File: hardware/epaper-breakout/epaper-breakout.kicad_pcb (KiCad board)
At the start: 2 copper layers, 100 x 40.5 mm, 90 parts, among them J1 XF2M-3315-1A, J2 C10418, J3 Conn_02x06_Counter_Clockwise, J4 ED060SC4, J5 Conn_01x01_Male, J6 Conn_01x01_Male, Q1 AO3401A, Q2 AO3401A, Q3 MMBT3904, Q4 MMBT3904, Q5 AO3401A, Q6 MMBT3904, U1 MCP1700-3302E_SOT23, U10 ED060SC7, U11 TP4056, U12 CH340C, U2 LT1945, U3 LT1945, U4 XC6206PxxxMR, U5 ESP32-WROVER, U6 ED060XC5, U7 LM358, U8 74HC4094-normal, U9 MCP9700AT-ETT

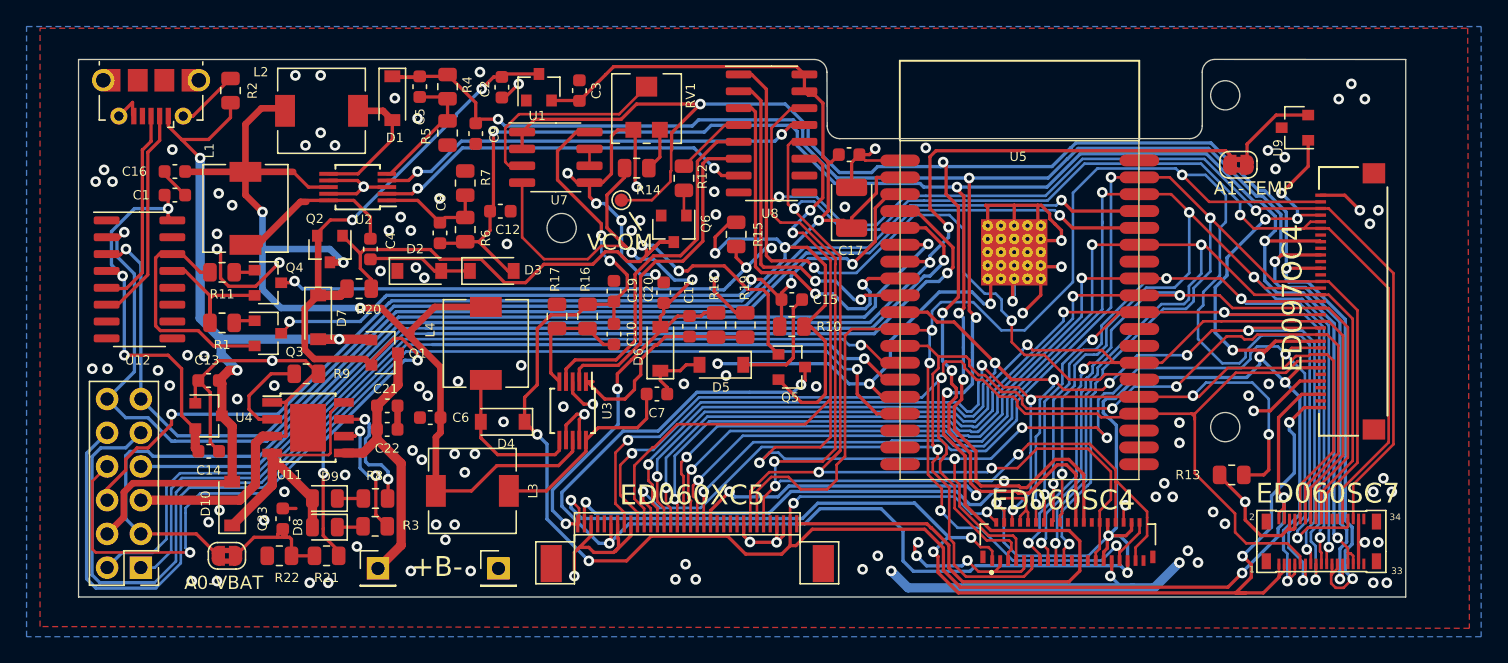
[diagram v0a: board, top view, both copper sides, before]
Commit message: minor change in V5
exchange L1 <-> U2 position
change usb connector footprint
change U6 footprint
chang RV1 footprint
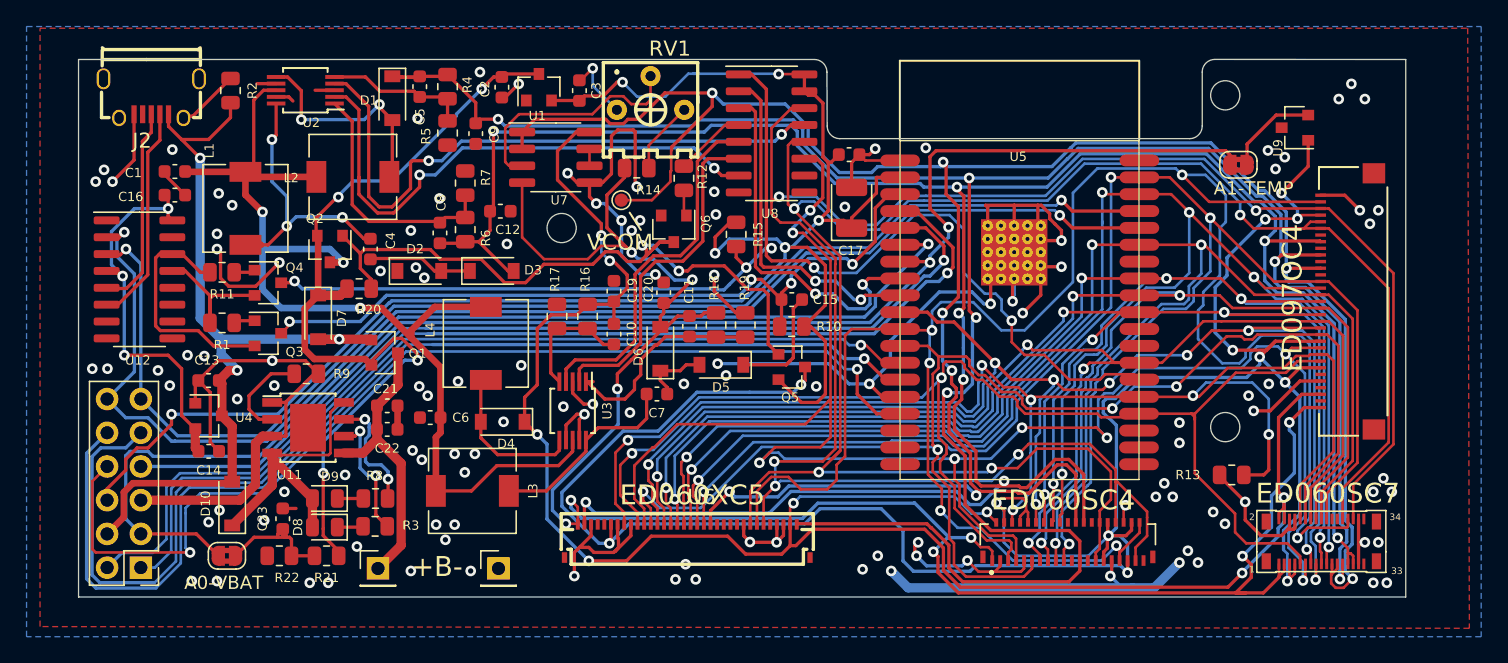
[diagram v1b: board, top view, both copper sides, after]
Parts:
- J2: footprint epaper-breakout:USB_Micro-B_A01SB141B1-067 -> epaper-breakout:JLC_MICRO-USB-SMD_A4A0507-E-01-R
- RV1: footprint epaper-breakout:EVM3ESX50B25 -> epaper-breakout:JLC_RES-ADJ-TH_3362P
- U6: footprint epaper-breakout:X05A20H34G -> epaper-breakout:JLC_FFC-SMD_34P-P0.50_FH34SRJ-34S-0.5SH
- moved U2 8.30 mm to (42.1, 21.8)
- moved L2 5.51 mm to (45.7, 28.3)
- moved J2 1.36 mm to (30.5, 22.4)
- moved U6 1.30 mm to (70.9, 55.8)
- moved RV1 1.22 mm to (68.1, 22.0), turned to 0 degrees
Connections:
- J1 pad 2: (no net) -> Net-(J1-Pad2)
- J1 pad 21: (no net) -> Net-(J1-Pad21)
- J1 pad 23: (no net) -> Net-(J1-Pad23)
- J1 pad 25: (no net) -> Net-(J1-Pad25)
- J1 pad 27: (no net) -> Net-(J1-Pad27)
- J1 pad 34: (no net) -> Net-(J1-Pad34)
- J1 pad 35: (no net) -> Net-(J1-Pad35)
- J1 pad 4: (no net) -> Net-(J1-Pad4)
- J1 pad 6: (no net) -> Net-(J1-Pad6)
- J2 pad 4: (no net) -> Net-(J2-Pad4)
- J4 pad 20: (no net) -> Net-(J4-Pad20)
- J4 pad 21: (no net) -> Net-(J4-Pad21)
- J4 pad 25: (no net) -> Net-(J4-Pad25)
- J4 pad 26: (no net) -> Net-(J4-Pad26)
- J4 pad 39: (no net) -> Net-(J4-Pad39)
- U10 pad 22: (no net) -> Net-(U10-Pad22)
- U10 pad 24: (no net) -> Net-(U10-Pad24)
- U10 pad 33: (no net) -> Net-(U10-Pad33)
- U10 pad 34: (no net) -> Net-(U10-Pad34)
- U11 pad 9: (no net) -> Net-(U11-Pad9)
- U12 pad 10: (no net) -> Net-(U12-Pad10)
- U12 pad 11: (no net) -> Net-(U12-Pad11)
- U12 pad 12: (no net) -> Net-(U12-Pad12)
- U12 pad 15: (no net) -> Net-(U12-Pad15)
- U12 pad 7: (no net) -> Net-(U12-Pad7)
- U12 pad 8: (no net) -> Net-(U12-Pad8)
- U12 pad 9: (no net) -> Net-(U12-Pad9)
- U5 pad 17: (no net) -> Net-(U5-Pad17)
- U5 pad 18: (no net) -> Net-(U5-Pad18)
- U5 pad 19: (no net) -> Net-(U5-Pad19)
- U5 pad 20: (no net) -> Net-(U5-Pad20)
- U5 pad 21: (no net) -> Net-(U5-Pad21)
- U5 pad 22: (no net) -> Net-(U5-Pad22)
- U5 pad 27: (no net) -> Net-(U5-Pad27)
- U5 pad 28: (no net) -> Net-(U5-Pad28)
- U5 pad 32: (no net) -> Net-(U5-Pad32)
- U6 pad 22: (no net) -> Net-(U6-Pad22)
- U6 pad 23: (no net) -> Net-(U6-Pad23)
- U6 pad 24: (no net) -> Net-(U6-Pad24)
- U6 pad 25: (no net) -> Net-(U6-Pad25)
- U6 pad 30: (no net) -> Net-(U6-Pad30)
- U6 pad 4: (no net) -> Net-(U6-Pad4)
- U6 pad 5: (no net) -> Net-(U6-Pad5)
- U8 pad 10: (no net) -> Net-(U8-Pad10)
- U8 pad 9: (no net) -> Net-(U8-Pad9)
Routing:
- net /CTRL+22V: track 33.2 -> 46.9 mm
- net /CTRL-20V: track 28.8 -> 41.4 mm
- net Net-(C8-Pad1): track 8.44 -> 19.1 mm
- net Net-(C4-Pad2): track 14.1 -> 22.8 mm, vias 0 -> 3
- net Net-(D1-Pad2): track 10.2 -> 16.8 mm, vias 0 -> 2
- net GND: track 262.0 -> 267.2 mm, vias 132 -> 124
- net Net-(R14-Pad2): track 3.23 -> 5.50 mm
- net /EP_VCOM: track 177.6 -> 179.8 mm
- net Net-(RV1-Pad2): track 15.9 -> 18.1 mm
- net Net-(C5-Pad1): track 10.0 -> 11.2 mm
- net VIN: track 63.1 -> 64.1 mm
- net /+3.3V: track 135.8 -> 136.6 mm, vias 4 -> 6
- net SW_VIN: track 80.1 -> 79.4 mm
